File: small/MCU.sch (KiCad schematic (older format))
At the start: 37 parts, among them IC1 PIC32MX350F256H-V_PT, J3 Micro_SD_Card, J4 Conn_01x05_Female, U5 AT25M02, U8 PCF8563T, Y2 Crystal

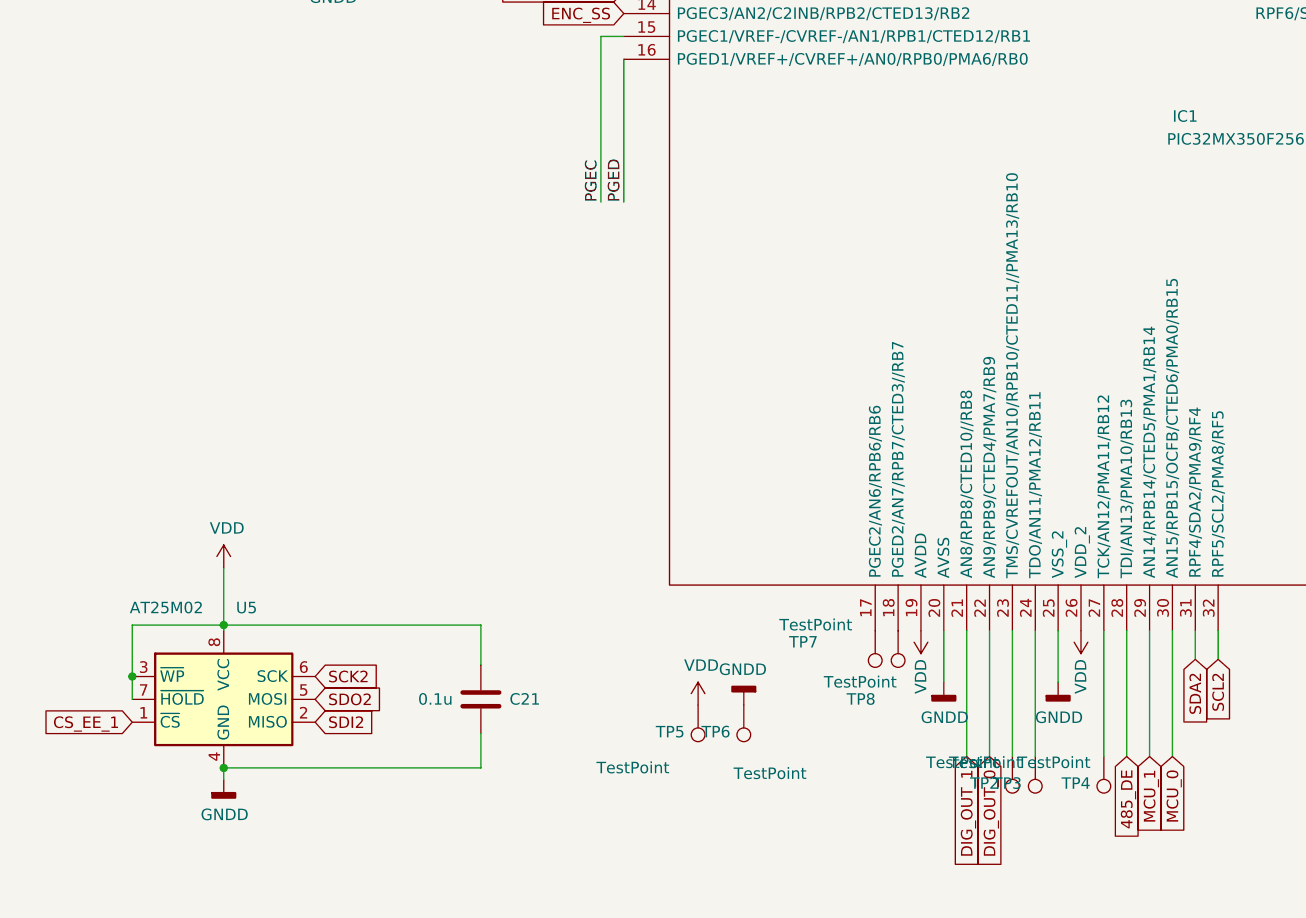
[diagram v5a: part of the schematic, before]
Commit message: accelerometer added
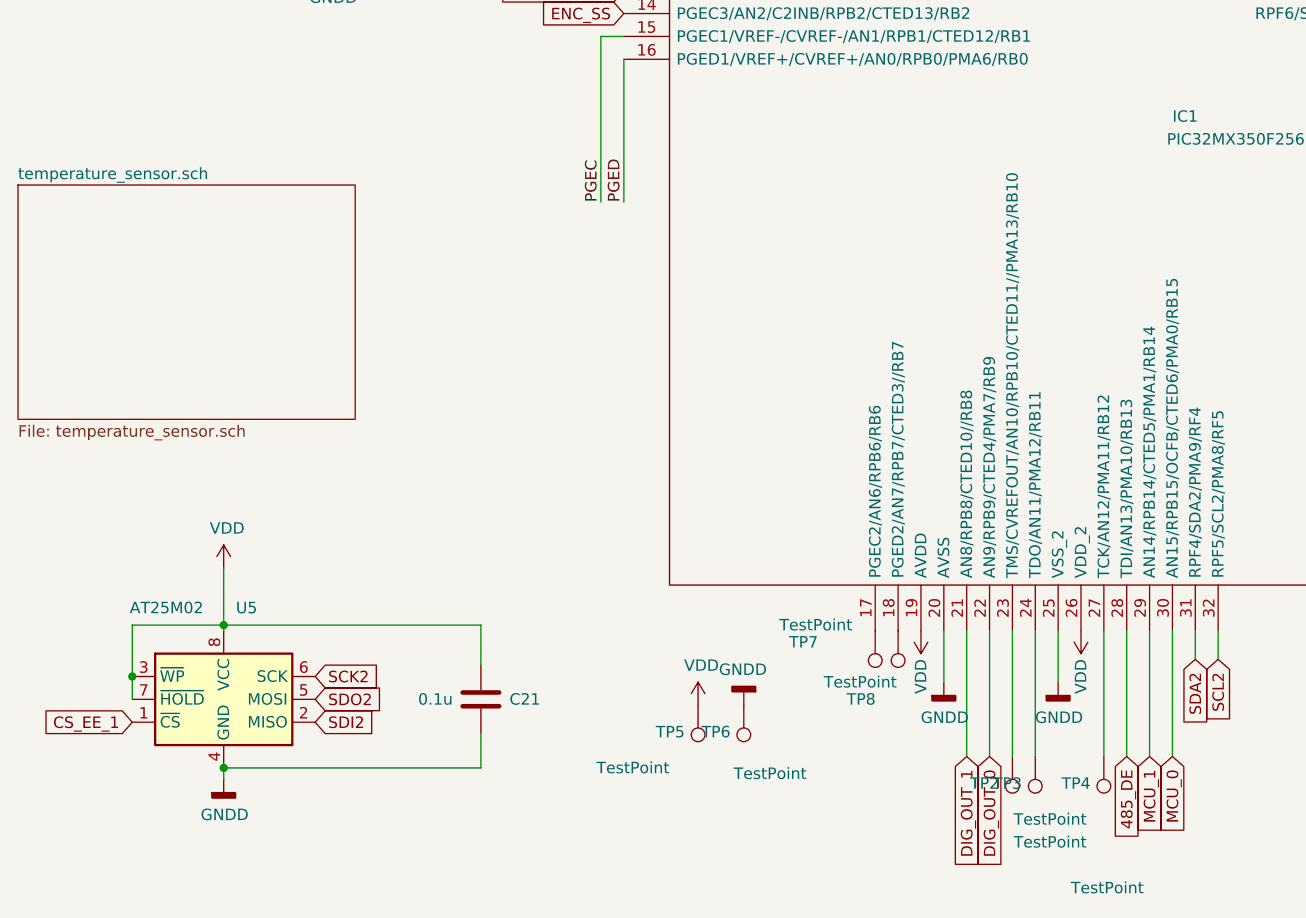
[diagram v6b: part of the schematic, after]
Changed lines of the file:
@@
 $Descr A4 11693 8268
 encoding utf-8
-Sheet 7 9
+Sheet 7 10
 Title ""
 Date ""
@@
 P 5100 7400
 F 0 "TP2" H 5158 7518 50  0000 L CNN
-F 1 "TestPoint" H 5158 7427 50  0000 L CNN
+F 1 "TestPoint" H 4775 7775 50  0000 L CNN
 F 2 "TestPoint:TestPoint_Pad_1.5x1.5mm" H 5300 7400 50  0001 C CNN
 F 3 "~" H 5300 7400 50  0001 C CNN
@@
 P 5200 7400
 F 0 "TP3" H 5258 7518 50  0000 L CNN
-F 1 "TestPoint" H 5258 7427 50  0000 L CNN
+F 1 "TestPoint" H 4975 7675 50  0000 L CNN
 F 2 "TestPoint:TestPoint_Pad_1.5x1.5mm" H 5400 7400 50  0001 C CNN
 F 3 "~" H 5400 7400 50  0001 C CNN
@@
 P 5500 7400
 F 0 "TP4" H 5558 7518 50  0000 L CNN
-F 1 "TestPoint" H 5558 7427 50  0000 L CNN
+F 1 "TestPoint" H 5325 7975 50  0000 L CNN
 F 2 "TestPoint:TestPoint_Pad_1.5x1.5mm" H 5700 7400 50  0001 C CNN
 F 3 "~" H 5700 7400 50  0001 C CNN
@@
 Wire Wire Line
 	11050 5500 11050 5550
+$Sheet
+S 750  4900 1475 1025
+U 603C60F5
+F0 "temperature_sensor.sch" 50
+F1 "temperature_sensor.sch" 50
+$EndSheet
 $EndSCHEMATC
